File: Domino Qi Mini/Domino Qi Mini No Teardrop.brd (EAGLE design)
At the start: 55.9 x 33 mm, 94 parts, among them J1 MH22-1, J2 MH22-1, M1 DOMINO, Q1 AP2302GN, Q2 2SC4081, SW1 IT-1210, SW2 IT-1210, SW3 IT-1210, U1 MP65151DJ, U2 ATMEGA32U4-AU/MU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

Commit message: Domino Qi Mini Rev. C: changed NTB0102GU to NTB0102GF
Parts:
- U5: value NTB0102GU -> NTB0102GF; device Domino:XQFN-10 -> Domino:SOT1089
- moved C21 3.30 mm to (15.6, 22.9), turned to 0 degrees
- moved C27 3.30 mm to (16.0, 25.5), turned to 0 degrees
- moved R19 2.99 mm to (17.8, 22.7), turned to 0 degrees
- moved R10 1.05 mm to (14.6, 24.4), turned to 270 degrees
- moved U5 0.13 mm to (16.8, 24.1), turned to 180 degrees
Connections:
- net +2V5: now also U5.3; no longer U5.2
- net +5V: now also U5.7; no longer U5.6
- net GND: now also U5.2; no longer U5.9
- net GP6: now also U5.1; no longer U5.5
- net I2S_MICIN: now also U5.6; no longer U5.4
- net I2S_WS: now also U5.5; no longer U5.10
- net JTAG_TDI: now also U5.4; no longer U5.1
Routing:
- net HANDSHAKE: track 32.8 -> 36.0 mm, vias 2 -> 3
- net GND: track 4.81 -> 6.56 mm, vias 234 -> 235
- net +2V5: track 37.8 -> 39.2 mm
- net LED8: track 16.0 -> 16.9 mm
- net I2S_WS: track 44.0 -> 44.7 mm
- net I2S_MICIN: track 50.5 -> 49.9 mm

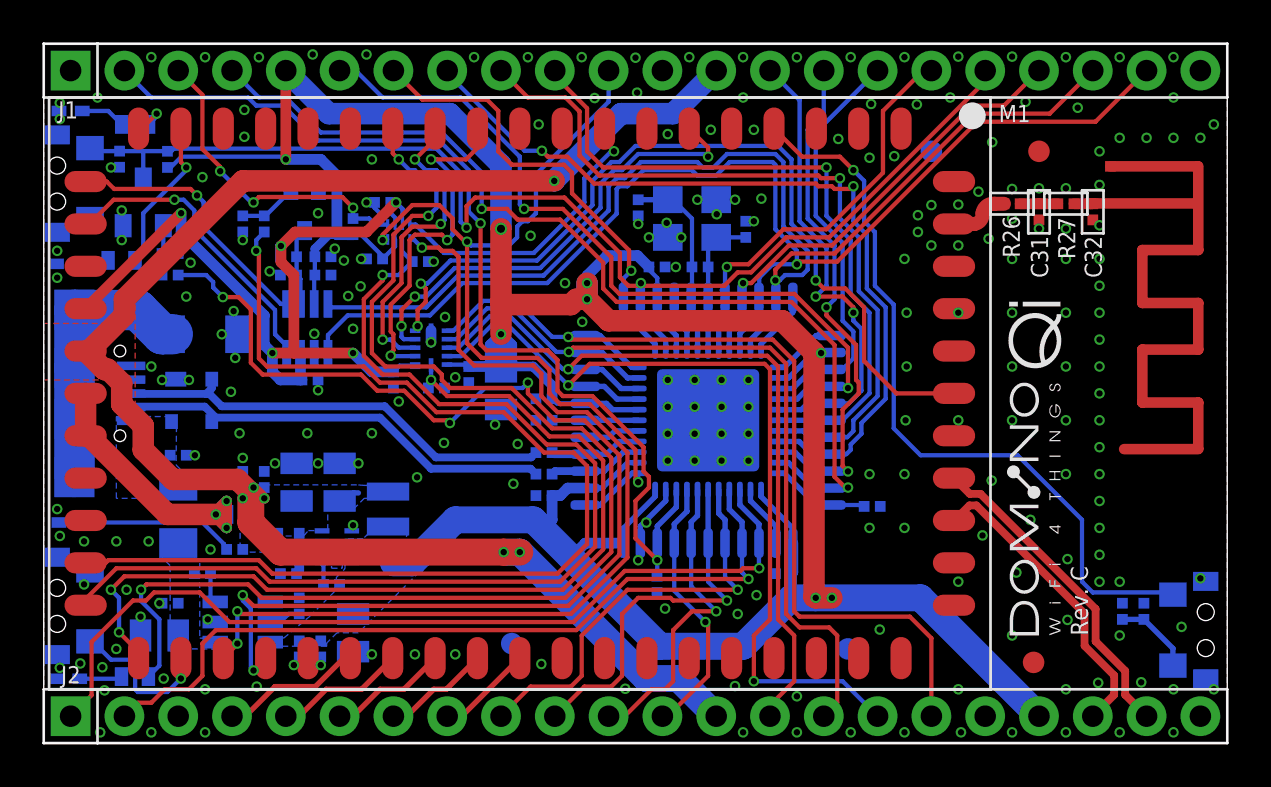
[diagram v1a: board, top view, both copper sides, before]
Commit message: Domino Qi Mini Rev. D: corrected bridge pinout
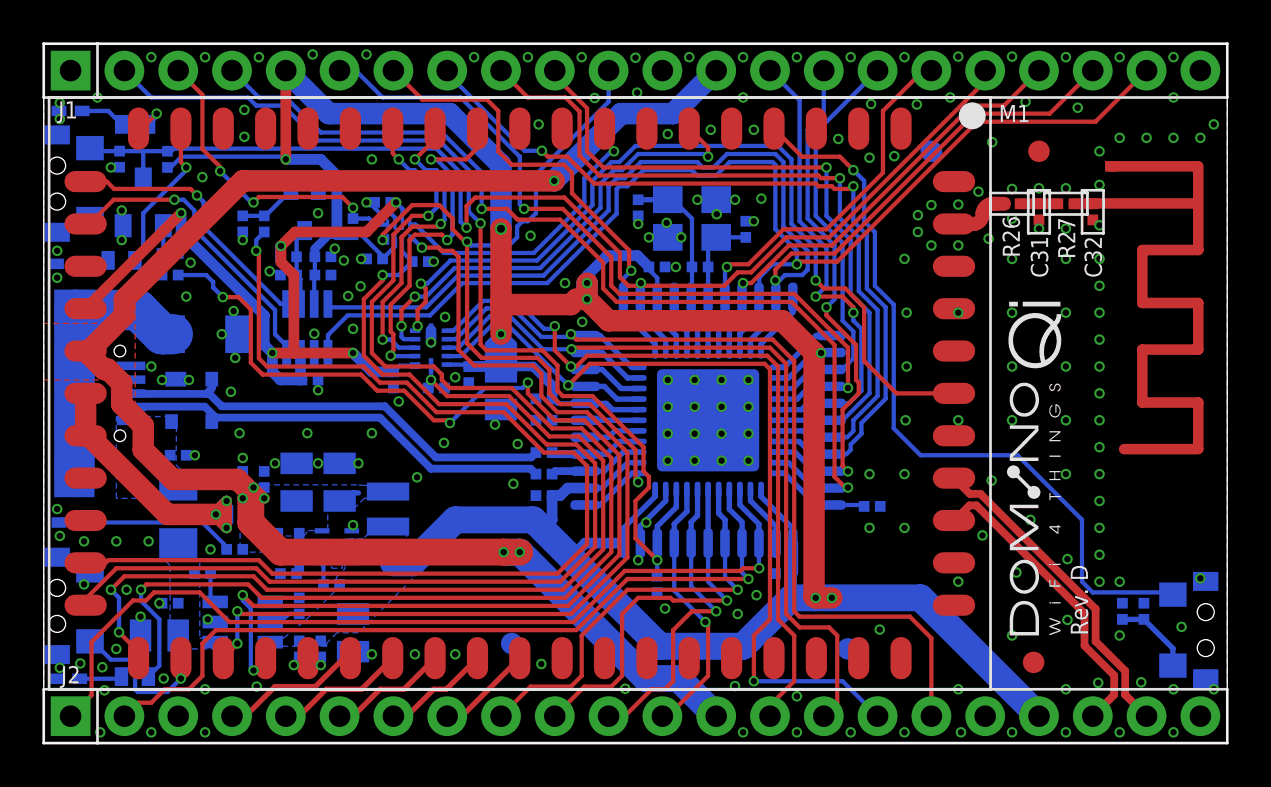
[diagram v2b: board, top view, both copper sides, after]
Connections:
- net MISO: now also U4.8; no longer U4.7
- net MOSI: now also U4.9; no longer U4.8
- net SCK: now also U4.7; no longer U4.9
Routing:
- net SCK: track 35.9 -> 36.7 mm, vias 1 -> 2
